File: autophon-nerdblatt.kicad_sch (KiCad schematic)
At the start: 21 parts, among them J101 board-edge-connector, U101 LM1117-3.3, U102 LM2594M-5.0

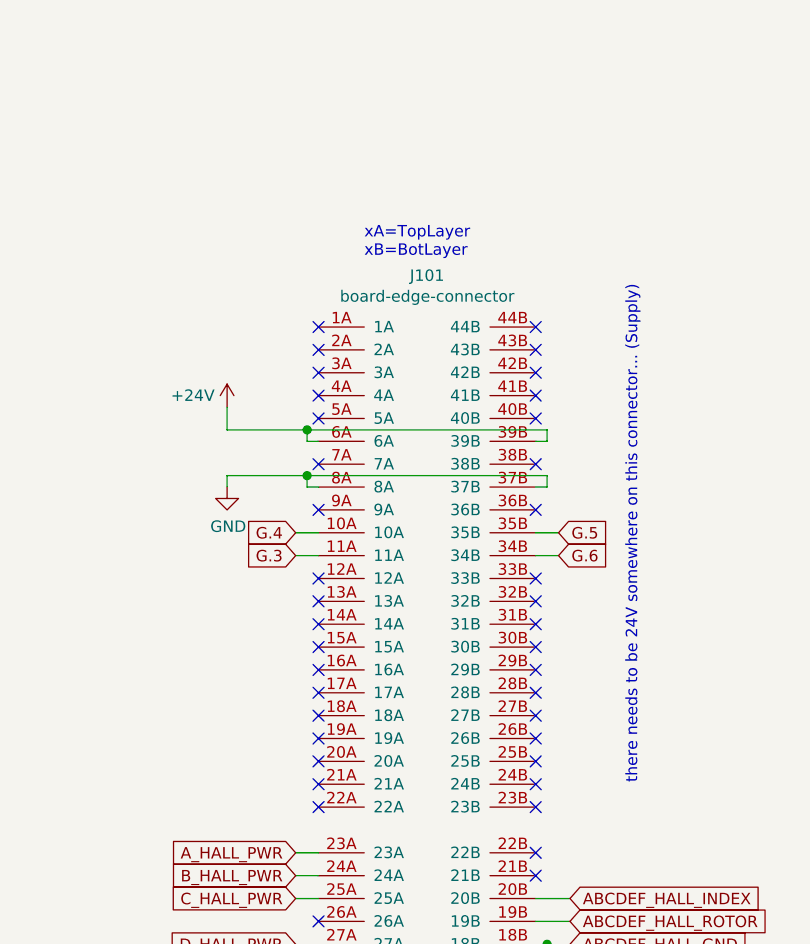
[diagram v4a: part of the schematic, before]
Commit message: Main schematic, unuglify main power.
+24V trace was crossing the main board connector which made
it almost impossible to select with kicad tools.
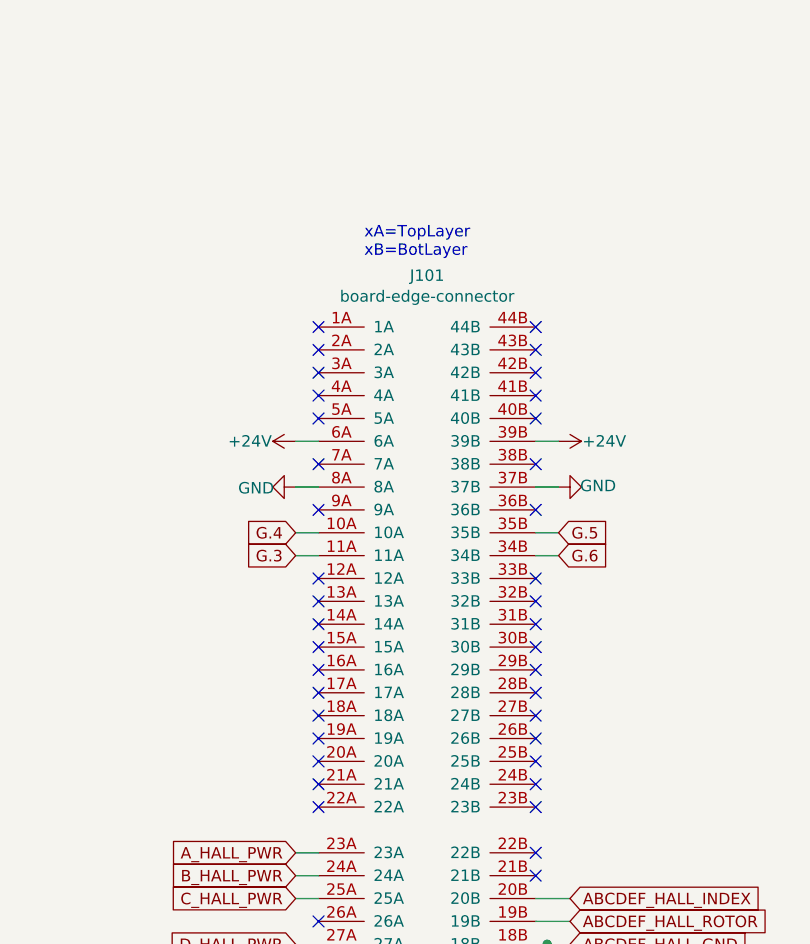
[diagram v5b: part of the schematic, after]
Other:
- note removed: "there needs to be 24V somewhere on this connector... (Supply)"
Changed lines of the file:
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@@
 (kicad_sch (version 20201015) (generator eeschema)
   (paper "A4")
-  (junction (at 86.36 59.69) (diameter 1.016) (color 0 0 0 0))
-  (junction (at 86.36 64.77) (diameter 1.016) (color 0 0 0 0))
   (junction (at 113.03 116.84) (diameter 1.016) (color 0 0 0 0))
   (junction (at 113.03 119.38) (diameter 1.016) (color 0 0 0 0))
@@
   (junction (at 248.92 38.1) (diameter 1.016) (color 0 0 0 0))
   (junction (at 257.81 38.1) (diameter 1.016) (color 0 0 0 0))
+  (no_connect (at 111.76 58.42))
+  (no_connect (at 111.76 48.26))
+  (no_connect (at 87.63 58.42))
+  (no_connect (at 87.63 83.82))
+  (no_connect (at 87.63 81.28))
+  (no_connect (at 111.76 157.48))
+  (no_connect (at 87.63 53.34))
+  (no_connect (at 87.63 114.3))
+  (no_connect (at 111.76 144.78))
+  (no_connect (at 87.63 149.86))
+  (no_connect (at 111.76 81.28))
+  (no_connect (at 111.76 152.4))
+  (no_connect (at 111.76 96.52))
+  (no_connect (at 111.76 91.44))
+  (no_connect (at 111.76 86.36))
+  (no_connect (at 111.76 68.58))
+  (no_connect (at 87.63 48.26))
+  (no_connect (at 111.76 99.06))
+  (no_connect (at 87.63 124.46))
+  (no_connect (at 87.63 88.9))
+  (no_connect (at 87.63 96.52))
+  (no_connect (at 111.76 93.98))
+  (no_connect (at 111.76 88.9))
+  (no_connect (at 87.63 91.44))
+  (no_connect (at 87.63 50.8))
+  (no_connect (at 111.76 149.86))
+  (no_connect (at 87.63 76.2))
+  (no_connect (at 87.63 68.58))
+  (no_connect (at 111.76 147.32))
+  (no_connect (at 87.63 160.02))
+  (no_connect (at 111.76 76.2))
+  (no_connect (at 111.76 160.02))
+  (no_connect (at 87.63 154.94))
+  (no_connect (at 111.76 53.34))
+  (no_connect (at 87.63 157.48))
   (no_connect (at 87.63 134.62))
+  (no_connect (at 87.63 101.6))
+  (no_connect (at 87.63 99.06))
   (no_connect (at 87.63 86.36))
-  (no_connect (at 111.76 160.02))
-  (no_connect (at 111.76 157.48))
-  (no_connect (at 111.76 86.36))
+  (no_connect (at 111.76 142.24))
+  (no_connect (at 87.63 152.4))
+  (no_connect (at 111.76 121.92))
+  (no_connect (at 111.76 83.82))
+  (no_connect (at 111.76 154.94))
+  (no_connect (at 87.63 93.98))
+  (no_connect (at 111.76 109.22))
+  (no_connect (at 111.76 50.8))
+  (no_connect (at 111.76 78.74))
+  (no_connect (at 111.76 55.88))
+  (no_connect (at 87.63 63.5))
+  (no_connect (at 111.76 63.5))
+  (no_connect (at 87.63 144.78))
+  (no_connect (at 87.63 147.32))
   (no_connect (at 111.76 101.6))
-  (no_connect (at 87.63 101.6))
-  (no_connect (at 87.63 160.02))
-  (no_connect (at 111.76 142.24))
-  (no_connect (at 111.76 68.58))
-  (no_connect (at 111.76 63.5))
-  (no_connect (at 111.76 53.34))
-  (no_connect (at 111.76 144.78))
-  (no_connect (at 87.63 91.44))
-  (no_connect (at 111.76 152.4))
-  (no_connect (at 87.63 157.48))
-  (no_connect (at 111.76 88.9))
-  (no_connect (at 111.76 121.92))
-  (no_connect (at 87.63 83.82))
-  (no_connect (at 111.76 93.98))
-  (no_connect (at 87.63 152.4))
-  (no_connect (at 111.76 78.74))
   (no_connect (at 111.76 106.68))
-  (no_connect (at 87.63 96.52))
-  (no_connect (at 111.76 96.52))
-  (no_connect (at 87.63 124.46))
-  (no_connect (at 87.63 76.2))
-  (no_connect (at 87.63 63.5))
-  (no_connect (at 111.76 55.88))
-  (no_connect (at 111.76 83.82))
+  (no_connect (at 111.76 124.46))
+  (no_connect (at 87.63 55.88))
   (no_connect (at 87.63 78.74))
-  (no_connect (at 87.63 53.34))
-  (no_connect (at 87.63 50.8))
-  (no_connect (at 87.63 81.28))
-  (no_connect (at 87.63 93.98))
-  (no_connect (at 87.63 58.42))
-  (no_connect (at 111.76 48.26))
-  (no_connect (at 111.76 147.32))
-  (no_connect (at 111.76 154.94))
-  (no_connect (at 87.63 114.3))
-  (no_connect (at 87.63 154.94))
-  (no_connect (at 111.76 50.8))
-  (no_connect (at 111.76 81.28))
-  (no_connect (at 111.76 76.2))
-  (no_connect (at 111.76 109.22))
-  (no_connect (at 87.63 99.06))
-  (no_connect (at 87.63 88.9))
-  (no_connect (at 111.76 99.06))
-  (no_connect (at 87.63 149.86))
-  (no_connect (at 87.63 144.78))
-  (no_connect (at 87.63 55.88))
-  (no_connect (at 111.76 91.44))
-  (no_connect (at 87.63 147.32))
-  (no_connect (at 111.76 58.42))
-  (no_connect (at 111.76 124.46))
-  (no_connect (at 87.63 68.58))
-  (no_connect (at 111.76 149.86))
-  (no_connect (at 87.63 48.26))
-  (wire (pts (xy 77.47 57.15) (xy 77.47 59.69))
-    (stroke (width 0) (type solid) (color 0 0 0 0))
-  )
-  (wire (pts (xy 77.47 59.69) (xy 86.36 59.69))
-    (stroke (width 0) (type solid) (color 0 0 0 0))
-  )
-  (wire (pts (xy 77.47 64.77) (xy 77.47 66.04))
+  (wire (pts (xy 85.09 60.96) (xy 87.63 60.96))
+    (stroke (width 0) (type solid) (color 0 0 0 0))
+  )
+  (wire (pts (xy 85.09 66.04) (xy 87.63 66.04))
     (stroke (width 0) (type solid) (color 0 0 0 0))
   )
@@
     (stroke (width 0) (type solid) (color 0 0 0 0))
   )
-  (wire (pts (xy 86.36 59.69) (xy 113.03 59.69))
-    (stroke (width 0) (type solid) (color 0 0 0 0))
-  )
-  (wire (pts (xy 86.36 60.96) (xy 86.36 59.69))
-    (stroke (width 0) (type solid) (color 0 0 0 0))
-  )
-  (wire (pts (xy 86.36 64.77) (xy 77.47 64.77))
-    (stroke (width 0) (type solid) (color 0 0 0 0))
-  )
-  (wire (pts (xy 86.36 64.77) (xy 113.03 64.77))
-    (stroke (width 0) (type solid) (color 0 0 0 0))
-  )
-  (wire (pts (xy 86.36 66.04) (xy 86.36 64.77))
-    (stroke (width 0) (type solid) (color 0 0 0 0))
-  )
-  (wire (pts (xy 87.63 60.96) (xy 86.36 60.96))
-    (stroke (width 0) (type solid) (color 0 0 0 0))
-  )
-  (wire (pts (xy 87.63 66.04) (xy 86.36 66.04))
+  (wire (pts (xy 111.76 60.96) (xy 114.3 60.96))
+    (stroke (width 0) (type solid) (color 0 0 0 0))
+  )
+  (wire (pts (xy 111.76 66.04) (xy 114.3 66.04))
     (stroke (width 0) (type solid) (color 0 0 0 0))
   )
@@
   )
   (wire (pts (xy 111.76 139.7) (xy 115.57 139.7))
-    (stroke (width 0) (type solid) (color 0 0 0 0))
-  )
-  (wire (pts (xy 113.03 59.69) (xy 113.03 60.96))
-    (stroke (width 0) (type solid) (color 0 0 0 0))
-  )
-  (wire (pts (xy 113.03 60.96) (xy 111.76 60.96))
-    (stroke (width 0) (type solid) (color 0 0 0 0))
-  )
-  (wire (pts (xy 113.03 64.77) (xy 113.03 66.04))
-    (stroke (width 0) (type solid) (color 0 0 0 0))
-  )
-  (wire (pts (xy 113.03 66.04) (xy 111.76 66.04))
     (stroke (width 0) (type solid) (color 0 0 0 0))
   )
@@
     (effects (font (size 1.27 1.27)) (justify left bottom))
   )
-  (text "there needs to be 24V somewhere on this connector... (Supply)"
-    (at 123.19 99.06 90)
-    (effects (font (size 1.27 1.27)) (justify left bottom))
-  )
   (text "(only global labels)" (at 229.87 160.02 0)
     (effects (font (size 1.27 1.27)) (justify left bottom))
@@
     )
   )
-  (symbol (lib_id "power:+24V") (at 77.47 57.15 0) (unit 1)
-    (in_bom yes) (on_board yes)
-    (property "Reference" "#PWR0109" (id 0) (at 77.47 60.96 0)
-      (effects (font (size 1.27 1.27)) hide)
-    )
-    (property "Value" "+24V" (id 1) (at 73.66 55.88 0))
-    (property "Footprint" "" (id 2) (at 77.47 57.15 0)
-      (effects (font (size 1.27 1.27)) hide)
-    )
-    (property "Datasheet" "" (id 3) (at 77.47 57.15 0)
+  (symbol (lib_id "power:+24V") (at 85.09 60.96 90) (unit 1)
+    (in_bom yes) (on_board yes)
+    (property "Reference" "#PWR0109" (id 0) (at 88.9 60.96 0)
+      (effects (font (size 1.27 1.27)) hide)
+    )
+    (property "Value" "+24V" (id 1) (at 80.01 60.96 90))
+    (property "Footprint" "" (id 2) (at 85.09 60.96 0)
+      (effects (font (size 1.27 1.27)) hide)
+    )
+    (property "Datasheet" "" (id 3) (at 85.09 60.96 0)
+      (effects (font (size 1.27 1.27)) hide)
+    )
+  )
+  (symbol (lib_id "power:+24V") (at 114.3 60.96 270) (unit 1)
+    (in_bom yes) (on_board yes)
+    (property "Reference" "#PWR?" (id 0) (at 110.49 60.96 0)
+      (effects (font (size 1.27 1.27)) hide)
+    )
+    (property "Value" "+24V" (id 1) (at 119.38 60.96 90))
+    (property "Footprint" "" (id 2) (at 114.3 60.96 0)
+      (effects (font (size 1.27 1.27)) hide)
+    )
+    (property "Datasheet" "" (id 3) (at 114.3 60.96 0)
       (effects (font (size 1.27 1.27)) hide)
     )
@@
     )
   )
-  (symbol (lib_id "power:GND") (at 77.47 66.04 0) (unit 1)
-    (in_bom yes) (on_board yes)
-    (property "Reference" "#PWR0108" (id 0) (at 77.47 72.39 0)
-      (effects (font (size 1.27 1.27)) hide)
-    )
-    (property "Value" "GND" (id 1) (at 77.597 70.4342 0))
-    (property "Footprint" "" (id 2) (at 77.47 66.04 0)
-      (effects (font (size 1.27 1.27)) hide)
-    )
-    (property "Datasheet" "" (id 3) (at 77.47 66.04 0)
+  (symbol (lib_id "power:GND") (at 85.09 66.04 270) (unit 1)
+    (in_bom yes) (on_board yes)
+    (property "Reference" "#PWR0108" (id 0) (at 78.74 66.04 0)
+      (effects (font (size 1.27 1.27)) hide)
+    )
+    (property "Value" "GND" (id 1) (at 80.6958 66.167 90))
+    (property "Footprint" "" (id 2) (at 85.09 66.04 0)
+      (effects (font (size 1.27 1.27)) hide)
+    )
+    (property "Datasheet" "" (id 3) (at 85.09 66.04 0)
+      (effects (font (size 1.27 1.27)) hide)
+    )
+  )
+  (symbol (lib_id "power:GND") (at 114.3 66.04 90) (unit 1)
+    (in_bom yes) (on_board yes)
+    (property "Reference" "#PWR?" (id 0) (at 120.65 66.04 0)
+      (effects (font (size 1.27 1.27)) hide)
+    )
+    (property "Value" "GND" (id 1) (at 118.6942 65.913 90))
+    (property "Footprint" "" (id 2) (at 114.3 66.04 0)
+      (effects (font (size 1.27 1.27)) hide)
+    )
+    (property "Datasheet" "" (id 3) (at 114.3 66.04 0)
       (effects (font (size 1.27 1.27)) hide)
     )
@@
       (reference "#PWR0113") (unit 1) (value "GND") (footprint "")
     )
+    (path "/3794d916-2190-4399-8aa5-c5be246e67ae"
+      (reference "#PWR?") (unit 1) (value "GND") (footprint "")
+    )
+    (path "/9e66ac77-6634-4d71-ad05-7921ce0c012e"
+      (reference "#PWR?") (unit 1) (value "+24V") (footprint "")
+    )
     (path "/00000000-0000-0000-0000-00006024444a"
